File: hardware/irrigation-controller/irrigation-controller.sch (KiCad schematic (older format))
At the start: 78 parts, among them J1 RS485, J10 I2C_2, J11 IO, J12 RELAY_2, J13 RELAY_3B, J14 RELAY_4B, J2 I2C_1, J3 ATMEGA ICSP, J4 ATMEGA UART, J5 RF Module, J6 PWR, J7 RELAY_1, J8 RELAY_3A, J9 RELAY_4A, K1 UA2-5NU, K2 UA2-5NU, Q1 MMBT3904, Q2 MMBT3904, Q3 2N7002, Q4 2N7002, Q5 2N7002, Q6 2N7002, SW1 SPST, U1 AQY280EH, U2 ATmega328P-AU, U3 AQY280EH, U4 TPS54331DR, U5 TPS54331DR, U6 MAX485, Y1 8MHz

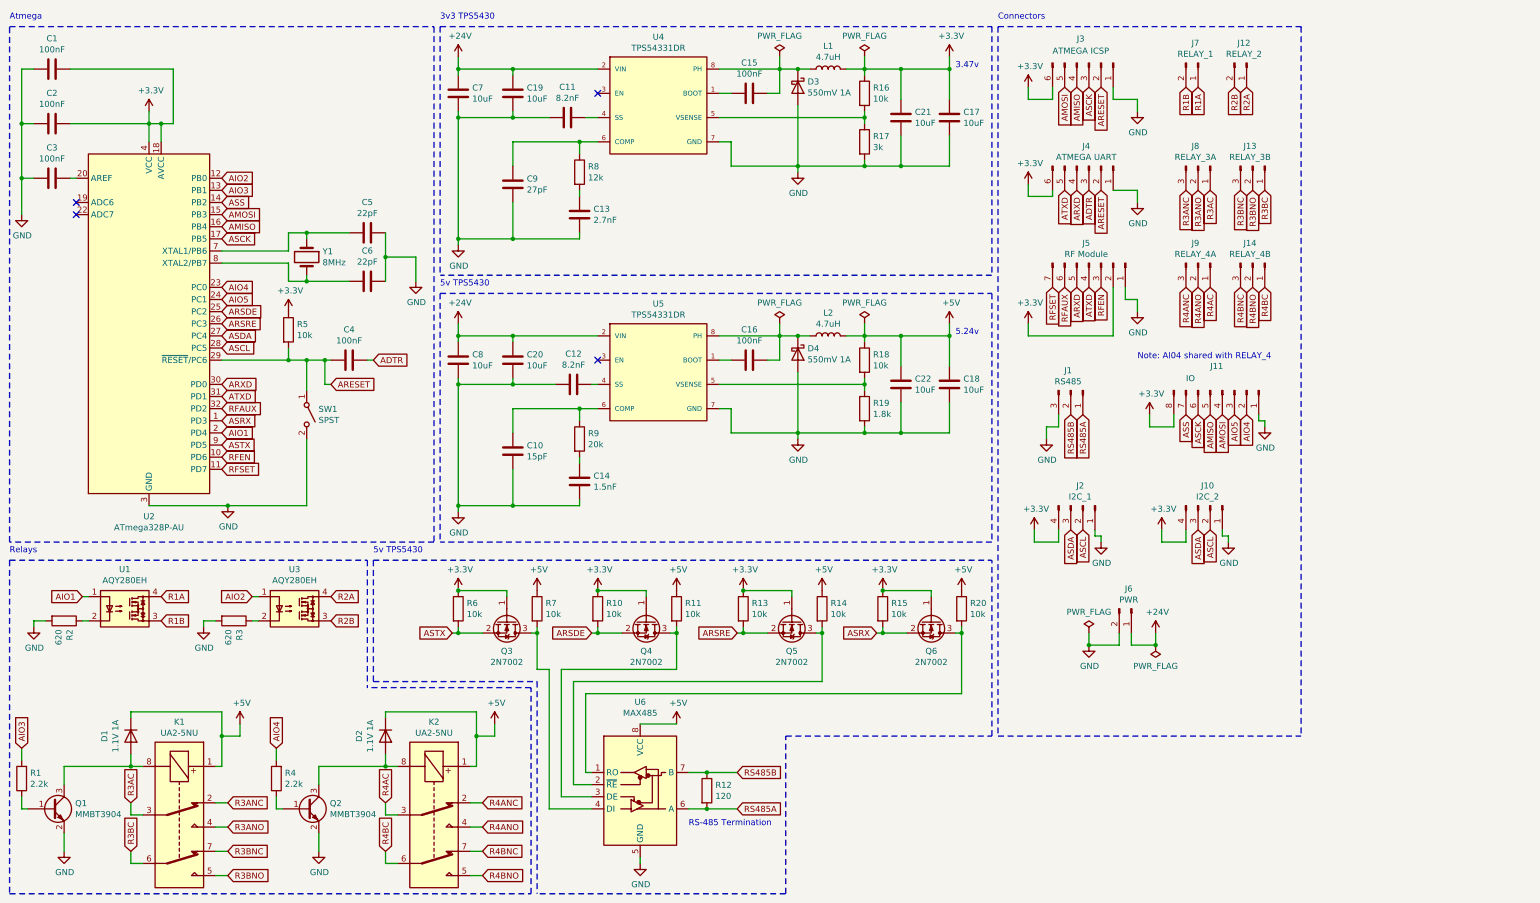
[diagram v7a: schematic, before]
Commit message: Add SW2 and FLOW header
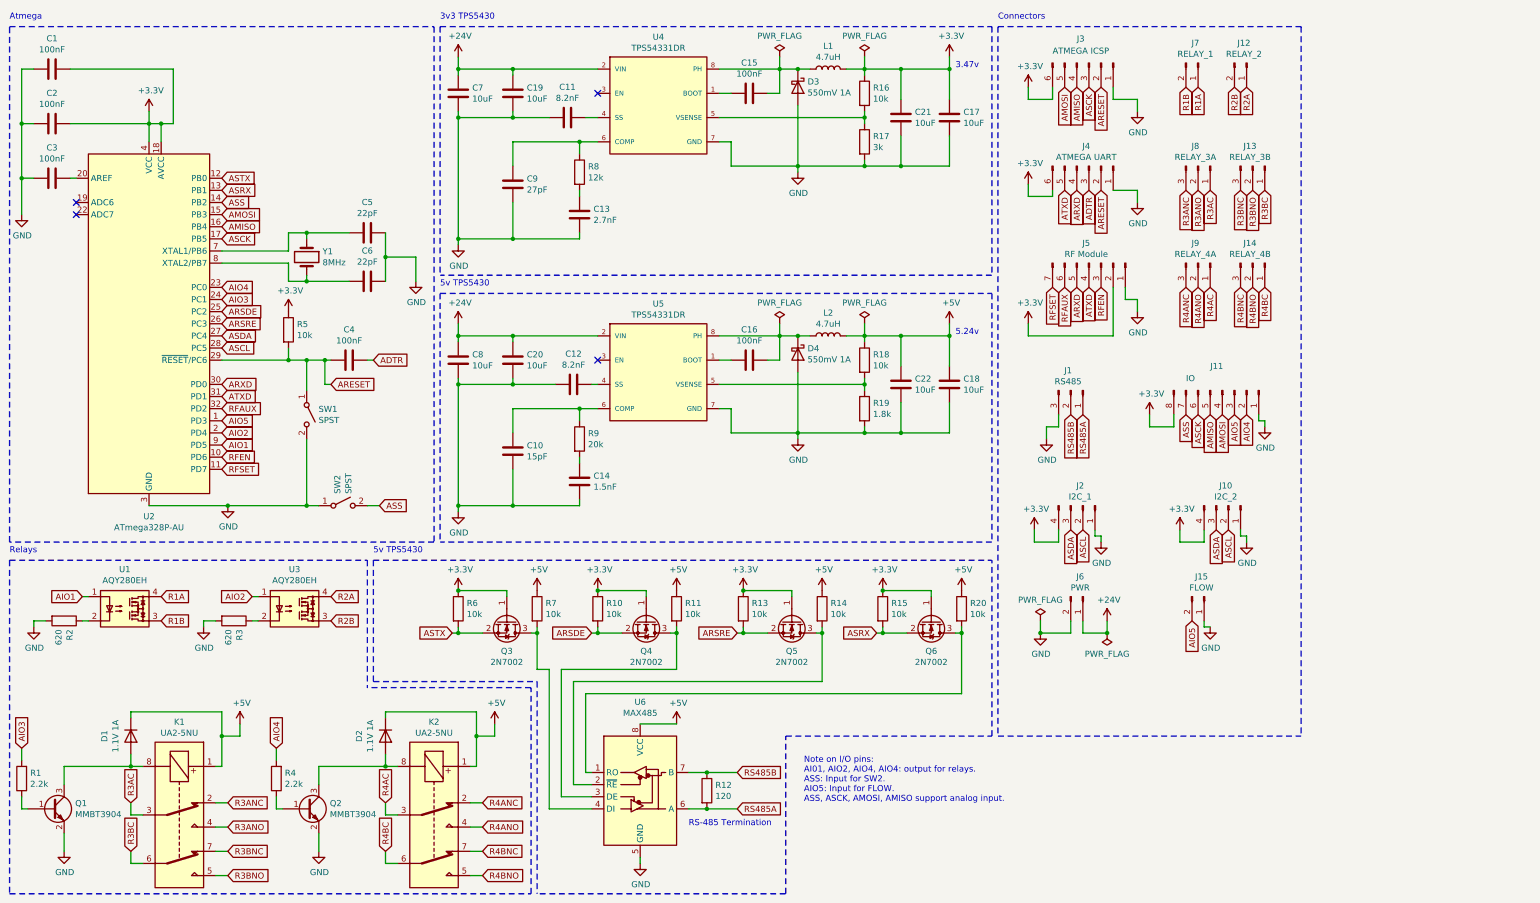
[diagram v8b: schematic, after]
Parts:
- added J15: FLOW, Connector_JST:JST_XH_B2B-XH-A_1x02_P2.50mm_Vertical, symbol Connector:Conn_01x02_Male
- added SW2: SPST, lib:SW_SPST_THT_5.0mm, symbol Switch:SW_SPST
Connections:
- net AIO1: now also U2.9 (PD5); no longer U2.2 (PD4)
- net AIO2: now also U2.2 (PD4); no longer U2.12 (PB0)
- net AIO3: now also U2.24 (PC1); no longer U2.13 (PB1)
- net AIO5: now also U2.1 (PD3), J15.2 (Pin_2); no longer U2.24 (PC1)
- net ASRX: now also U2.13 (PB1); no longer U2.1 (PD3)
- net ASS: now also SW2.2 (B)
- net ASTX: now also U2.12 (PB0); no longer U2.9 (PD5)
- net GND: now also J15.1 (Pin_1), SW2.1 (A)
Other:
- note added: "Note on I/O pins:\nAI01, AIO2, AIO4, AIO4: output for relays.\nASS: Input for SW2.\nAIO5: Input for FLOW.\nASS, ASCK, AMOSI, AMISO support analog input."
- note removed: "Note: AI04 shared with RELAY_4"
- moved on the sheet: J10, J6
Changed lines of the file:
@@
 Text GLabel 1750 5500 2    50   Input ~ 0
 R1B
-Text GLabel 2250 3950 2    50   Input ~ 0
+Text GLabel 2250 4050 2    50   Input ~ 0
 AIO1
 $Comp
@@
 Text GLabel 3150 5500 2    50   Input ~ 0
 R2B
-Text GLabel 2250 1850 2    50   Input ~ 0
+Text GLabel 2250 3950 2    50   Input ~ 0
 AIO2
 $Comp
@@
 	-1   0    0    1
 $EndComp
+Text GLabel 2250 2850 2    50   Input ~ 0
+AIO3
 Text GLabel 2250 1950 2    50   Input ~ 0
-AIO3
-Text GLabel 2250 3850 2    50   Input ~ 0
 ASRX
-Text GLabel 2250 4050 2    50   Input ~ 0
+Text GLabel 2250 1850 2    50   Input ~ 0
 ASTX
 Text GLabel 4150 5600 0    50   Input ~ 0
@@
 Text GLabel 2250 2750 2    50   Input ~ 0
 AIO4
-Text GLabel 2250 2850 2    50   Input ~ 0
+Text GLabel 2250 3850 2    50   Input ~ 0
 AIO5
 Text GLabel 6500 6750 2    50   Input ~ 0
@@
 	0    1    1    0
 $EndComp
-Text Notes 9800 3350 0    50   ~ 0
-Note: AI04 shared with RELAY_4
-Text GLabel 10300 4750 3    50   Input ~ 0
+Text Notes 7050 7000 0    50   ~ 0
+Note on I/O pins:\nAI01, AIO2, AIO4, AIO4: output for relays.\nASS: Input for SW2.\nAIO5: Input for FLOW.\nASS, ASCK, AMOSI, AMISO support analog input.
+Text GLabel 10450 4750 3    50   Input ~ 0
 ASDA
-Text GLabel 10400 4750 3    50   Input ~ 0
+Text GLabel 10550 4750 3    50   Input ~ 0
 ASCL
 $Comp
 L Connector:Conn_01x04_Male J10
 U 1 1 618BA1F4
-P 10400 4550
-F 0 "J10" V 10235 4528 50  0000 C CNN
-F 1 "I2C_2" V 10326 4528 50  0000 C CNN
-F 2 "Connector_JST:JST_XH_B4B-XH-A_1x04_P2.50mm_Vertical" H 10400 4550 50  0001 C CNN
-F 3 "~" H 10400 4550 50  0001 C CNN
-F 4 "https://au.mouser.com/ProductDetail/426-FIT0255" V 10400 4550 50  0001 C CNN "Purchase Link"
-	1    10400 4550
+P 10550 4550
+F 0 "J10" V 10385 4528 50  0000 C CNN
+F 1 "I2C_2" V 10476 4528 50  0000 C CNN
+F 2 "Connector_JST:JST_XH_B4B-XH-A_1x04_P2.50mm_Vertical" H 10550 4550 50  0001 C CNN
+F 3 "~" H 10550 4550 50  0001 C CNN
+F 4 "https://au.mouser.com/ProductDetail/426-FIT0255" V 10550 4550 50  0001 C CNN "Purchase Link"
+	1    10550 4550
 	0    1    1    0
 $EndComp
@@
 L power:+3.3V #PWR042
 U 1 1 618BA1FE
-P 10000 4750
-F 0 "#PWR042" H 10000 4600 50  0001 C CNN
-F 1 "+3.3V" H 10015 4923 50  0000 C CNN
-F 2 "" H 10000 4750 50  0001 C CNN
-F 3 "" H 10000 4750 50  0001 C CNN
-	1    10000 4750
-	1    0    0    -1
-$EndComp
-Wire Wire Line
-	10000 4750 10000 4850
-Wire Wire Line
-	10000 4850 10200 4850
-Wire Wire Line
-	10200 4850 10200 4750
+P 10150 4750
+F 0 "#PWR042" H 10150 4600 50  0001 C CNN
+F 1 "+3.3V" H 10165 4923 50  0000 C CNN
+F 2 "" H 10150 4750 50  0001 C CNN
+F 3 "" H 10150 4750 50  0001 C CNN
+	1    10150 4750
+	1    0    0    -1
+$EndComp
+Wire Wire Line
+	10150 4750 10150 4850
+Wire Wire Line
+	10150 4850 10350 4850
+Wire Wire Line
+	10350 4850 10350 4750
 $Comp
 L power:GND #PWR043
 U 1 1 618BA20B
-P 10550 4850
-F 0 "#PWR043" H 10550 4600 50  0001 C CNN
-F 1 "GND" H 10555 4677 50  0000 C CNN
-F 2 "" H 10550 4850 50  0001 C CNN
-F 3 "" H 10550 4850 50  0001 C CNN
-	1    10550 4850
-	1    0    0    -1
-$EndComp
-Wire Wire Line
-	10500 4750 10500 4800
-Wire Wire Line
-	10500 4800 10550 4800
-Wire Wire Line
-	10550 4800 10550 4850
+P 10700 4850
+F 0 "#PWR043" H 10700 4600 50  0001 C CNN
+F 1 "GND" H 10705 4677 50  0000 C CNN
+F 2 "" H 10700 4850 50  0001 C CNN
+F 3 "" H 10700 4850 50  0001 C CNN
+	1    10700 4850
+	1    0    0    -1
+$EndComp
+Wire Wire Line
+	10650 4750 10650 4800
+Wire Wire Line
+	10650 4800 10700 4800
+Wire Wire Line
+	10700 4800 10700 4850
 Wire Notes Line
 	8650 6450 11150 6450
@@
 L power:PWR_FLAG #FLG04
 U 1 1 61923EF8
-P 9950 5700
-F 0 "#FLG04" H 9950 5775 50  0001 C CNN
-F 1 "PWR_FLAG" H 9950 5873 50  0000 C CNN
-F 2 "" H 9950 5700 50  0001 C CNN
-F 3 "~" H 9950 5700 50  0001 C CNN
-	1    9950 5700
+P 9550 5600
+F 0 "#FLG04" H 9550 5675 50  0001 C CNN
+F 1 "PWR_FLAG" H 9550 5773 50  0000 C CNN
+F 2 "" H 9550 5600 50  0001 C CNN
+F 3 "~" H 9550 5600 50  0001 C CNN
+	1    9550 5600
 	-1   0    0    1
 $EndComp
@@
 L power:+24V #PWR041
 U 1 1 61924F74
-P 9950 5600
-F 0 "#PWR041" H 9950 5450 50  0001 C CNN
-F 1 "+24V" H 9965 5773 50  0000 C CNN
-F 2 "" H 9950 5600 50  0001 C CNN
-F 3 "" H 9950 5600 50  0001 C CNN
-	1    9950 5600
+P 9550 5500
+F 0 "#PWR041" H 9550 5350 50  0001 C CNN
+F 1 "+24V" H 9565 5673 50  0000 C CNN
+F 2 "" H 9550 5500 50  0001 C CNN
+F 3 "" H 9550 5500 50  0001 C CNN
+	1    9550 5500
 	1    0    0    -1
 $EndComp
@@
 L Connector:Conn_01x02_Male J6
 U 1 1 61926C7F
-P 9750 5400
-F 0 "J6" V 9585 5378 50  0000 C CNN
-F 1 "PWR" V 9676 5378 50  0000 C CNN
-F 2 "Connector_JST:JST_XH_B2B-XH-A_1x02_P2.50mm_Vertical" H 9750 5400 50  0001 C CNN
-F 3 "~" H 9750 5400 50  0001 C CNN
-F 4 "https://au.mouser.com/ProductDetail/426-FIT0255" V 9750 5400 50  0001 C CNN "Purchase Link"
-	1    9750 5400
-	0    1    1    0
-$EndComp
-Wire Wire Line
-	9750 5600 9750 5700
-Wire Wire Line
-	9750 5700 9950 5700
-Wire Wire Line
-	9950 5700 9950 5600
-Connection ~ 9950 5700
+P 9350 5300
+F 0 "J6" V 9185 5278 50  0000 C CNN
+F 1 "PWR" V 9276 5278 50  0000 C CNN
+F 2 "Connector_JST:JST_XH_B2B-XH-A_1x02_P2.50mm_Vertical" H 9350 5300 50  0001 C CNN
+F 3 "~" H 9350 5300 50  0001 C CNN
+F 4 "https://au.mouser.com/ProductDetail/426-FIT0255" V 9350 5300 50  0001 C CNN "Purchase Link"
+	1    9350 5300
+	0    1    1    0
+$EndComp
+Wire Wire Line
+	9350 5500 9350 5600
+Wire Wire Line
+	9350 5600 9550 5600
+Wire Wire Line
+	9550 5600 9550 5500
+Connection ~ 9550 5600
 $Comp
 L power:GND #PWR035
 U 1 1 61962CBA
-P 9400 5700
-F 0 "#PWR035" H 9400 5450 50  0001 C CNN
-F 1 "GND" H 9405 5527 50  0000 C CNN
-F 2 "" H 9400 5700 50  0001 C CNN
-F 3 "" H 9400 5700 50  0001 C CNN
-	1    9400 5700
+P 9000 5600
+F 0 "#PWR035" H 9000 5350 50  0001 C CNN
+F 1 "GND" H 9005 5427 50  0000 C CNN
+F 2 "" H 9000 5600 50  0001 C CNN
+F 3 "" H 9000 5600 50  0001 C CNN
+	1    9000 5600
 	1    0    0    -1
 $EndComp
@@
 L power:PWR_FLAG #FLG03
 U 1 1 619D5328
-P 9400 5600
-F 0 "#FLG03" H 9400 5675 50  0001 C CNN
-F 1 "PWR_FLAG" H 9400 5773 50  0000 C CNN
-F 2 "" H 9400 5600 50  0001 C CNN
-F 3 "~" H 9400 5600 50  0001 C CNN
-	1    9400 5600
-	1    0    0    -1
-$EndComp
-Wire Wire Line
-	9400 5600 9400 5700
-Wire Wire Line
-	9650 5600 9650 5700
-Wire Wire Line
-	9650 5700 9400 5700
-Connection ~ 9400 5700
+P 9000 5500
+F 0 "#FLG03" H 9000 5575 50  0001 C CNN
+F 1 "PWR_FLAG" H 9000 5673 50  0000 C CNN
+F 2 "" H 9000 5500 50  0001 C CNN
+F 3 "~" H 9000 5500 50  0001 C CNN
+	1    9000 5500
+	1    0    0    -1
+$EndComp
+Wire Wire Line
+	9000 5500 9000 5600
+Wire Wire Line
+	9250 5500 9250 5600
+Wire Wire Line
+	9250 5600 9000 5600
+Connection ~ 9000 5600
 $Comp
 L power:PWR_FLAG #FLG01
@@
 Wire Wire Line
 	7850 3950 7550 3950
+Text GLabel 3550 4550 2    50   Input ~ 0
+ASS
+$Comp
+L Switch:SW_SPST SW2
+U 1 1 6141924A
+P 3250 4550
+F 0 "SW2" V 3204 4648 50  0000 L CNN
+F 1 "SPST" V 3295 4648 50  0000 L CNN
+F 2 "lib:SW_SPST_THT_5.0mm" H 3250 4550 50  0001 C CNN
+F 3 "https://www.farnell.com/datasheets/3176355.pdf" H 3250 4550 50  0001 C CNN
+F 4 "" H 3250 4550 50  0001 C CNN "Purchase link"
+F 5 "https://au.element14.com/multicomp-pro/mc32879/switch-tactile-spst-no-50ma-though/dp/171299401" H 3250 4550 50  0001 C CNN "Purchase Link"
+	1    3250 4550
+	1    0    0    -1
+$EndComp
+Wire Wire Line
+	3550 4550 3450 4550
+Wire Wire Line
+	3050 4550 2950 4550
+Connection ~ 2950 4550
+$Comp
+L Connector:Conn_01x02_Male J15
+U 1 1 614A1089
+P 10350 5300
+F 0 "J15" V 10185 5278 50  0000 C CNN
+F 1 "FLOW" V 10276 5278 50  0000 C CNN
+F 2 "Connector_JST:JST_XH_B2B-XH-A_1x02_P2.50mm_Vertical" H 10350 5300 50  0001 C CNN
+F 3 "~" H 10350 5300 50  0001 C CNN
+F 4 "https://au.mouser.com/ProductDetail/426-FIT0255" V 10350 5300 50  0001 C CNN "Purchase Link"
+	1    10350 5300
+	0    1    1    0
+$EndComp
+Text GLabel 10250 5500 3    50   Input ~ 0
+AIO5
+$Comp
+L power:GND #PWR0101
+U 1 1 61508FEE
+P 10400 5550
+F 0 "#PWR0101" H 10400 5300 50  0001 C CNN
+F 1 "GND" H 10405 5377 50  0000 C CNN
+F 2 "" H 10400 5550 50  0001 C CNN
+F 3 "" H 10400 5550 50  0001 C CNN
+	1    10400 5550
+	1    0    0    -1
+$EndComp
+Wire Wire Line
+	10400 5550 10350 5550
+Wire Wire Line
+	10350 5550 10350 5500
 $EndSCHEMATC
